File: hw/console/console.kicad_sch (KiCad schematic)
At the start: 126 parts, among them J1 Batt, J301 USB-C 16P, J401 microSD push-push, J601 FFC-40 0.5mm, Q601 N-MOSFET, SW1 Движок, SW2 RESET, SW301 FEL, U1 F133-A, U2 SY8089AAAC, U3 SY8089AAAC, U4 SY8089AAAC, U401 W25Q32JVSSIQ, U5 TP4056, Y1 24 МГц, Y2 32.768 кГц

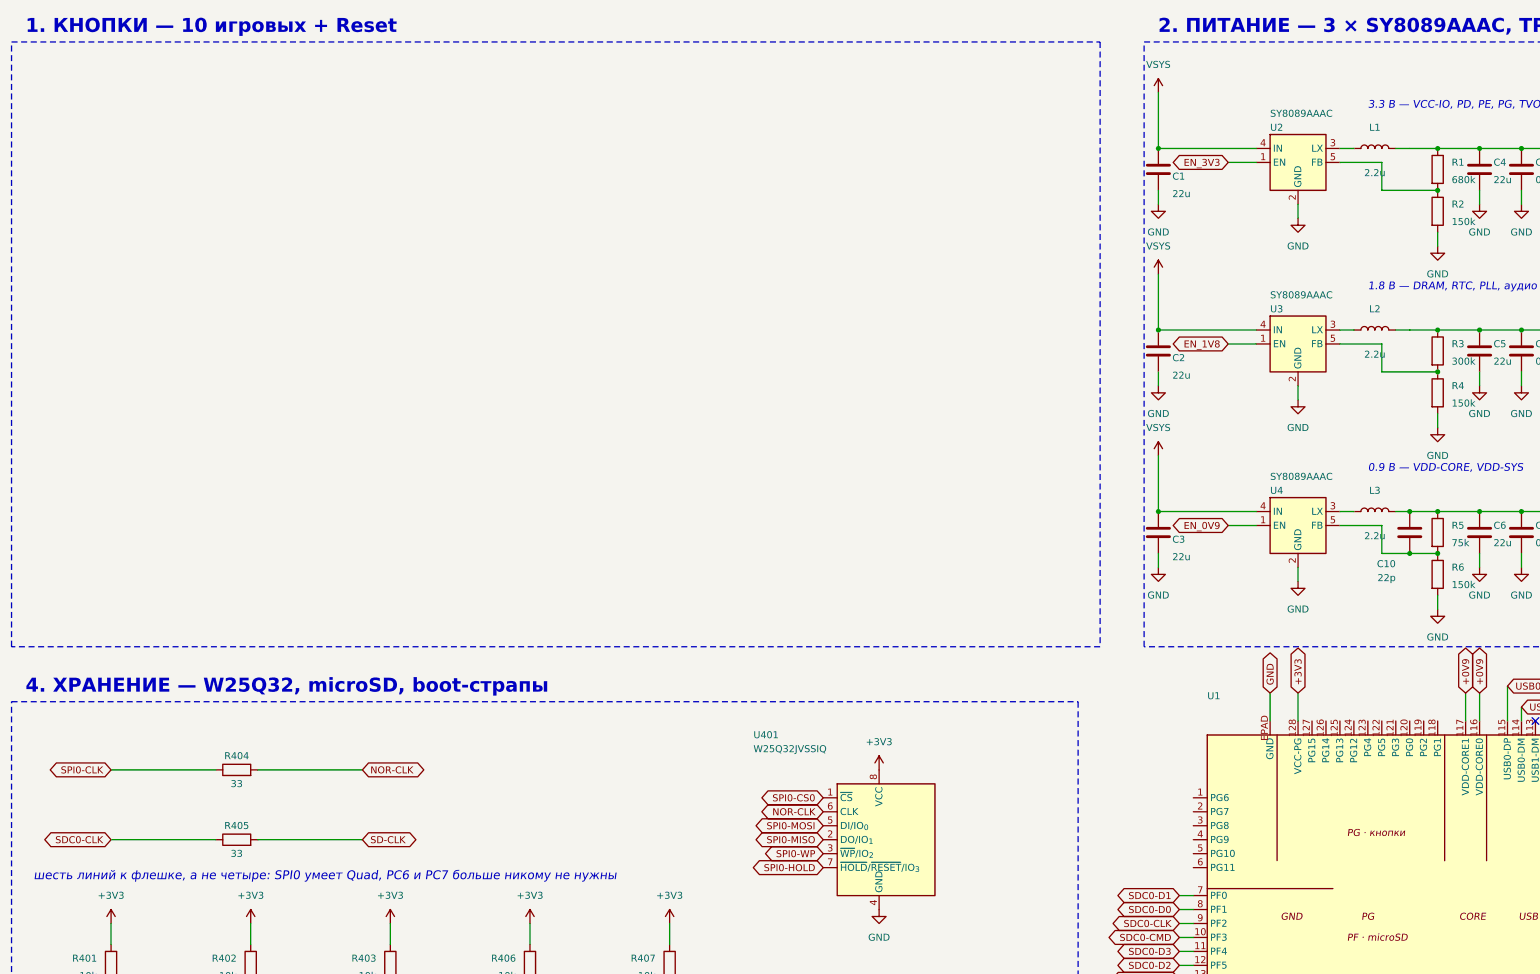
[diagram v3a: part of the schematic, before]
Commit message: hw: блок 1 «Кнопки» — документ и чертёж
Десять кнопок на PG6..PG15, ни одной пассивной детали: подтяжка вверх у F133
внутренняя. Референса у блока нет — ни MangoPi, ни Xassette игровых кнопок не
имеют, — поэтому все решения опираются на Table 5-4 и user manual, а цена
ошибки вынесена в допущения.

PG0..PG5 оставлены свободными: это единственная целая шина SDC1, и MangoPi
вешает на неё Wi-Fi. Крестики «не подключать» ставит блок 8.

Co-Authored-By: Claude Opus 5 <noreply@anthropic.com>
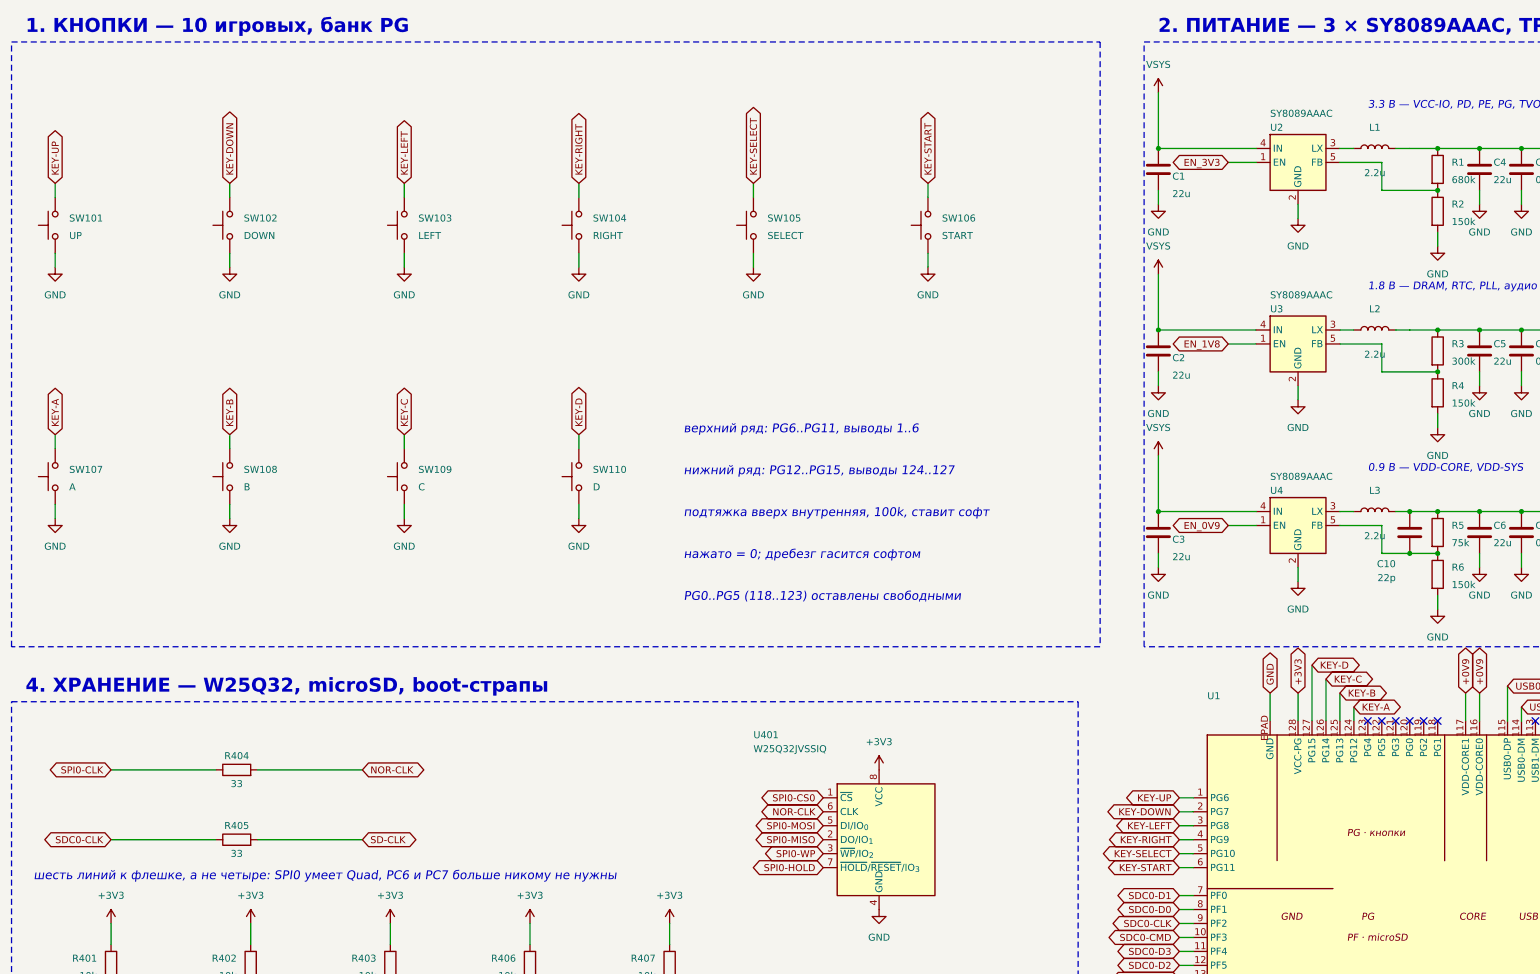
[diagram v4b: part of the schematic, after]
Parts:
- added SW101: UP, Button_Switch_SMD:SW_SPST_PTS645Sx43SMTR92, symbol Switch:SW_Push
- added SW102: DOWN, Button_Switch_SMD:SW_SPST_PTS645Sx43SMTR92, symbol Switch:SW_Push
- added SW103: LEFT, Button_Switch_SMD:SW_SPST_PTS645Sx43SMTR92, symbol Switch:SW_Push
- added SW104: RIGHT, Button_Switch_SMD:SW_SPST_PTS645Sx43SMTR92, symbol Switch:SW_Push
- added SW105: SELECT, Button_Switch_SMD:SW_SPST_PTS645Sx43SMTR92, symbol Switch:SW_Push
- added SW106: START, Button_Switch_SMD:SW_SPST_PTS645Sx43SMTR92, symbol Switch:SW_Push
- added SW107: A, Button_Switch_SMD:SW_SPST_PTS645Sx43SMTR92, symbol Switch:SW_Push
- added SW108: B, Button_Switch_SMD:SW_SPST_PTS645Sx43SMTR92, symbol Switch:SW_Push
- added SW109: C, Button_Switch_SMD:SW_SPST_PTS645Sx43SMTR92, symbol Switch:SW_Push
- added SW110: D, Button_Switch_SMD:SW_SPST_PTS645Sx43SMTR92, symbol Switch:SW_Push
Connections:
- net GND: now also SW101.1, SW102.1, SW103.1, SW104.1, SW105.1, SW106.1, SW107.1, SW108.1, SW109.1, SW110.1
- net KEY-UP: now reaches U1.1 (PG6)
- net KEY-UP: now also SW101.2
- net KEY-A: now reaches U1.124 (PG12)
- net KEY-A: now also SW107.2
- net KEY-B: now reaches U1.125 (PG13)
- net KEY-B: now also SW108.2
- net KEY-C: now reaches U1.126 (PG14)
- net KEY-C: now also SW109.2
- net KEY-D: now reaches U1.127 (PG15)
- net KEY-D: now also SW110.2
- net KEY-DOWN: now reaches U1.2 (PG7)
- net KEY-DOWN: now also SW102.2
- net KEY-LEFT: now reaches U1.3 (PG8)
- net KEY-LEFT: now also SW103.2
- net KEY-RIGHT: now reaches U1.4 (PG9)
- net KEY-RIGHT: now also SW104.2
- net KEY-SELECT: now reaches U1.5 (PG10)
- net KEY-SELECT: now also SW105.2
- net KEY-START: now reaches U1.6 (PG11)
- net KEY-START: now also SW106.2
- no-connect marks 10 -> 16
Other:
- note added: "1. КНОПКИ — 10 игровых, банк PG"
- note added: "PG0..PG5 (118..123) оставлены свободными"
- note added: "верхний ряд: PG6..PG11, выводы 1..6"
- note added: "нажато = 0; дребезг гасится софтом"
- note added: "нижний ряд: PG12..PG15, выводы 124..127"
- note added: "подтяжка вверх внутренняя, 100k, ставит софт"
- note removed: "1. КНОПКИ — 10 игровых + Reset"

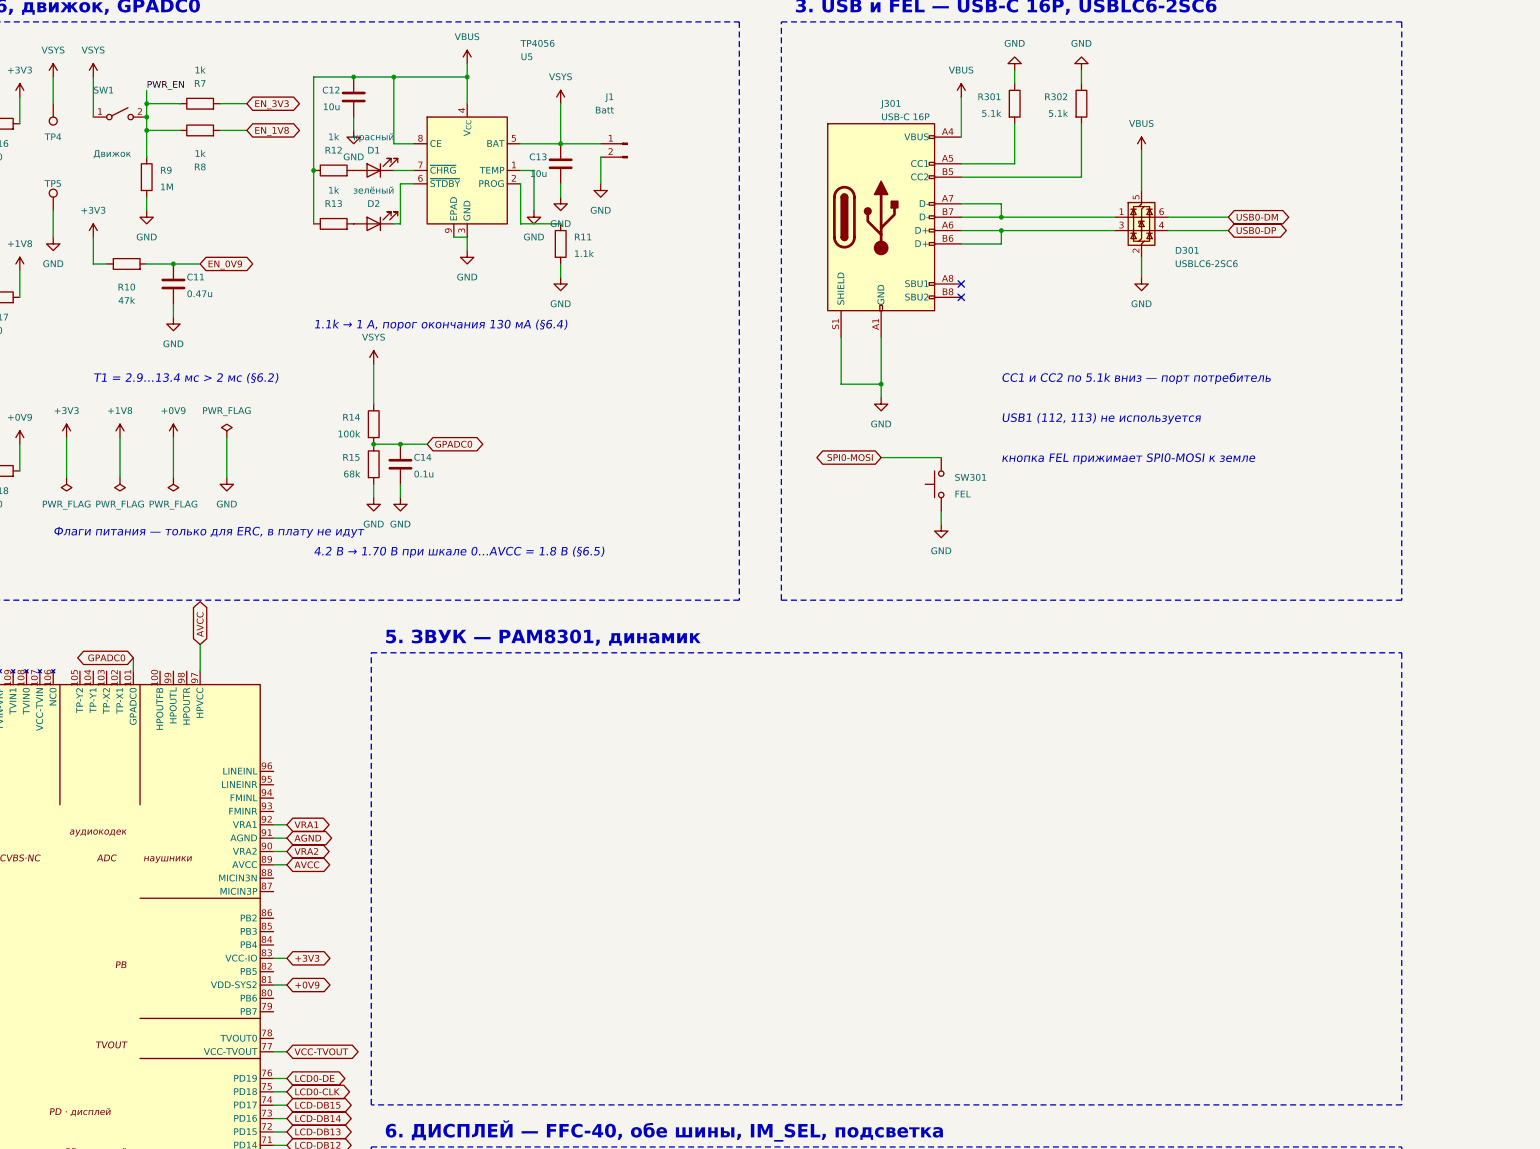
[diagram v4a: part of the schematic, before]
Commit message: hw: блок 5 «Звук» — документ и чертёж
Кодек F133 -> сумматор 47k -> PAM8301 -> динамик 8 Ом. Одиннадцать деталей.

Три расхождения с MangoPi, все посчитаны: сумматор 47k вместо 150k (иначе
0.13 Вт вместо 0.83), SD на GPIO с подтяжкой вниз вместо перемычки на питание
(VSYS живёт всегда, усилитель иначе ест 4 мА при выключенной консоли), земля
усилителя на GND вместо AGND.

Заодно закрыт флаг питания VBUS, обещанный ещё блоком 3: выводы разъёма для
ERC passive, и цепь считалась незапитанной.

Co-Authored-By: Claude Opus 5 <noreply@anthropic.com>
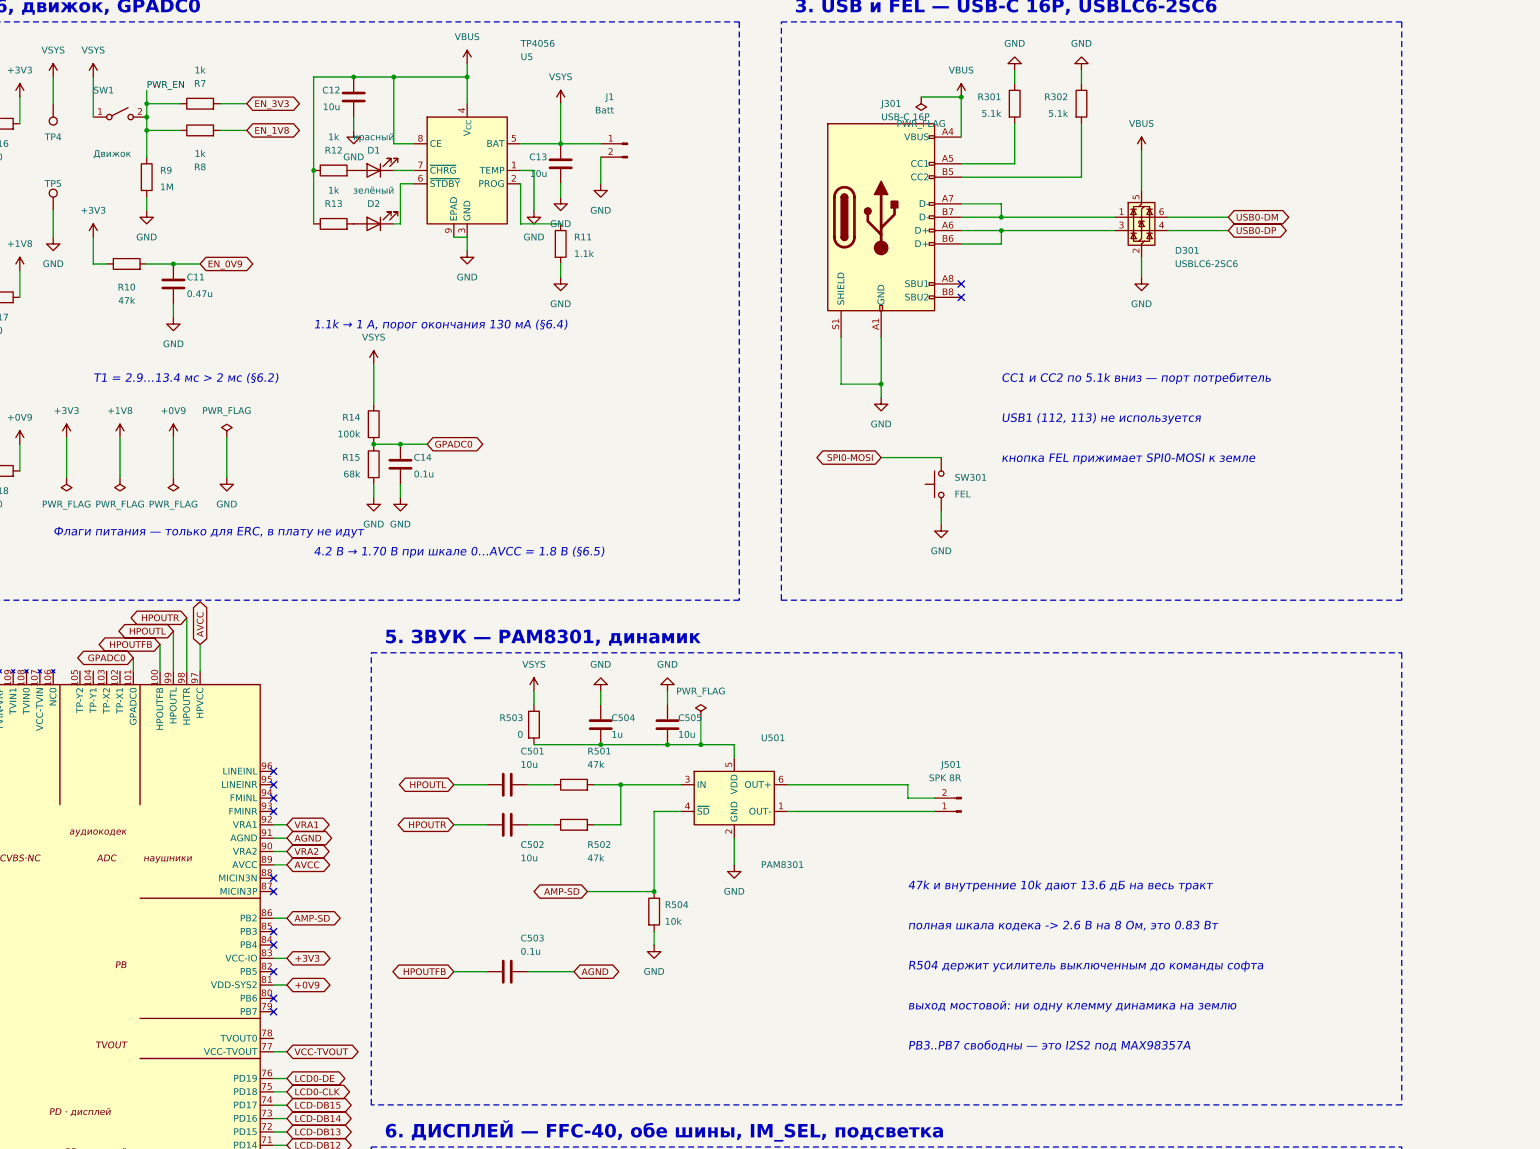
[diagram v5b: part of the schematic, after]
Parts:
- added C501, C502, C505: 10u, Capacitor_SMD:C_0805_2012Metric_Pad1.18x1.45mm_HandSolder, symbol Device:C
- added C503: 0.1u, Capacitor_SMD:C_0805_2012Metric_Pad1.18x1.45mm_HandSolder, symbol Device:C
- added C504: 1u, Capacitor_SMD:C_0805_2012Metric_Pad1.18x1.45mm_HandSolder, symbol Device:C
- added J501: SPK 8R, Connector_PinHeader_2.54mm:PinHeader_1x02_P2.54mm_Vertical, symbol Connector:Conn_01x02_Pin
- added R501, R502: 47k, Resistor_SMD:R_0805_2012Metric_Pad1.20x1.40mm_HandSolder, symbol Device:R
- added R503: 0, Resistor_SMD:R_0805_2012Metric_Pad1.20x1.40mm_HandSolder, symbol Device:R
- added R504: 10k, Resistor_SMD:R_0805_2012Metric_Pad1.20x1.40mm_HandSolder, symbol Device:R
- added U501: PAM8301, Package_TO_SOT_SMD:SOT-23-6, symbol Amplifier_Audio:PAM8301
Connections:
- net AGND: now also C503.2
- net GND: now also C504.1, C505.1, R504.2, U501.2 (GND)
- net VSYS: now also R503.1
- net HPOUTFB: now reaches U1.100 (HPOUTFB)
- net HPOUTFB: now also C503.1
- net AMP-SD: now reaches U1.86 (PB2)
- net AMP-SD: now also R504.1, U501.4 (~{SD})
- net HPOUTR: now reaches U1.98 (HPOUTR)
- net HPOUTR: now also C502.1
- net HPOUTL: now reaches U1.99 (HPOUTL)
- net HPOUTL: now also C501.1
- new net: C501.2, R501.1
- new net: R501.2, R502.2, U501.3 (IN)
- new net: C504.2, C505.2, R503.2, U501.5 (VDD)
- new net: J501.1 (Pin_1), U501.1 (OUT-)
- new net: J501.2 (Pin_2), U501.6 (OUT+)
- new net: C502.2, R502.1
- no-connect marks 16 -> 27
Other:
- note added: "47k и внутренние 10k дают 13.6 дБ на весь тракт"
- note added: "PB3..PB7 свободны — это I2S2 под MAX98357A"
- note added: "R504 держит усилитель выключенным до команды софта"
- note added: "выход мостовой: ни одну клемму динамика на землю"
- note added: "полная шкала кодека -> 2.6 В на 8 Ом, это 0.83 Вт"
